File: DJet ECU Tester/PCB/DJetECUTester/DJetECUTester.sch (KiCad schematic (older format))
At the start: 25 parts, among them J1 ISP, J2 ECU, J4 BREAKOUT, J5 12V IN, J6 MPS, U1 ATmega328P, Y1 FA-238 16.0000MB-C3

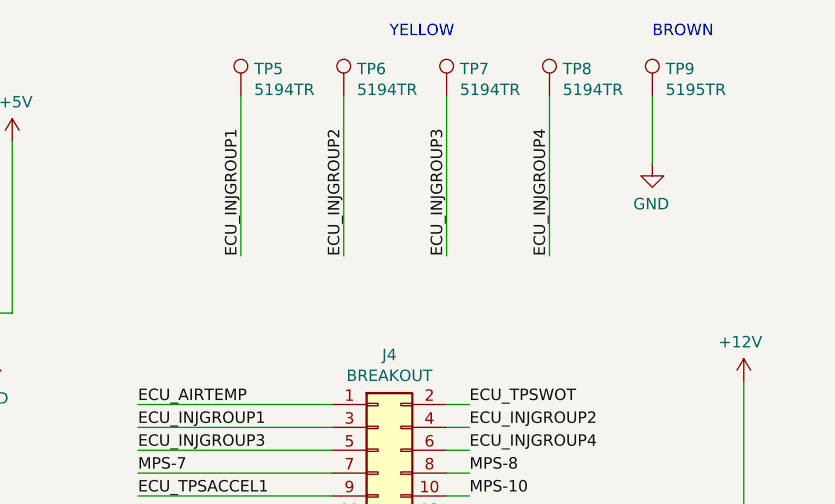
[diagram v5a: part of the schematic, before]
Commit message: Added simulation of injector drivers - only 1-5 group tested.
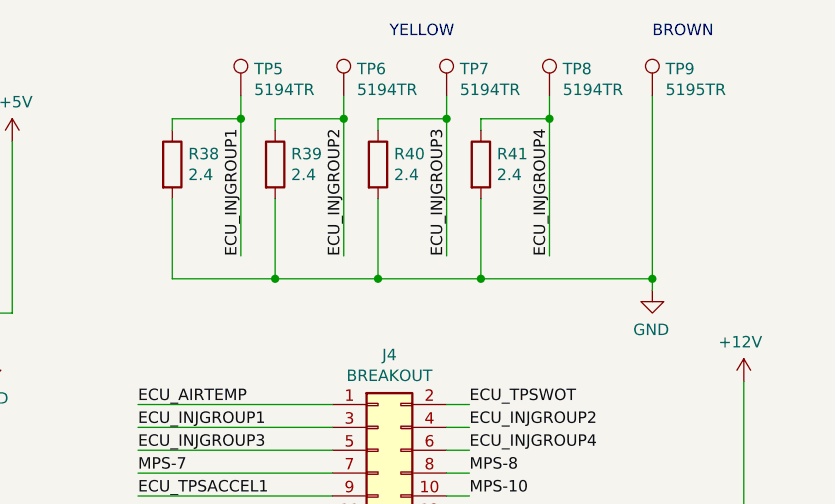
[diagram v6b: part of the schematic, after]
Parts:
- added R38, R39, R40, R41: 2.4, Resistor_SMD:R_0805_2012Metric, symbol Device:R
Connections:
- net ECU_INJGROUP1: now also R38.1
- net ECU_INJGROUP2: now also R39.1
- net ECU_INJGROUP3: now also R40.1
- net ECU_INJGROUP4: now also R41.1
- net GND: now also R38.2, R39.2, R40.2, R41.2
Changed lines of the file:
@@
 L power:GND #PWR053
 U 1 1 60447C04
-P 9650 1200
+P 9650 1750
 AR Path="/60447C04" Ref="#PWR053"  Part="1"
 AR Path="/60479334/60447C04" Ref="#PWR?"  Part="1"
-F 0 "#PWR053" H 9650 950 50  0001 C CNN
-F 1 "GND" H 9655 1027 50  0000 C CNN
-F 2 "" H 9650 1200 50  0001 C CNN
-F 3 "" H 9650 1200 50  0001 C CNN
-	1    9650 1200
+F 0 "#PWR053" H 9650 1500 50  0001 C CNN
+F 1 "GND" H 9655 1577 50  0000 C CNN
+F 2 "" H 9650 1750 50  0001 C CNN
+F 3 "" H 9650 1750 50  0001 C CNN
+	1    9650 1750
 	-1   0    0    -1
 $EndComp
-Wire Wire Line
-	9650 1200 9650 900
 Text Label 7850 1600 1    50   ~ 0
 ECU_INJGROUP1
@@
 ECU_INJGROUP4
 Wire Wire Line
-	7850 900  7850 1600
+	7850 900  7850 1000
 Wire Wire Line
-	8300 900  8300 1600
+	8300 900  8300 1000
 Wire Wire Line
-	8750 900  8750 1600
+	8750 900  8750 1000
 Wire Wire Line
-	9200 900  9200 1600
+	9200 900  9200 1000
 $Sheet
 S 1500 3850 900  300
@@
 Text Notes 8500 650  0    50   ~ 0
 YELLOW
+$Comp
+L Device:R R38
+U 1 1 604C75AB
+P 7550 1200
+F 0 "R38" H 7620 1246 50  0000 L CNN
+F 1 "2.4" H 7620 1155 50  0000 L CNN
+F 2 "Resistor_SMD:R_0805_2012Metric" V 7480 1200 50  0001 C CNN
+F 3 "~" H 7550 1200 50  0001 C CNN
+	1    7550 1200
+	1    0    0    -1
+$EndComp
+Wire Wire Line
+	7850 1000 7550 1000
+Wire Wire Line
+	7550 1000 7550 1050
+Connection ~ 7850 1000
+Wire Wire Line
+	7850 1000 7850 1600
+$Comp
+L Device:R R39
+U 1 1 604D383D
+P 8000 1200
+F 0 "R39" H 8070 1246 50  0000 L CNN
+F 1 "2.4" H 8070 1155 50  0000 L CNN
+F 2 "Resistor_SMD:R_0805_2012Metric" V 7930 1200 50  0001 C CNN
+F 3 "~" H 8000 1200 50  0001 C CNN
+	1    8000 1200
+	1    0    0    -1
+$EndComp
+$Comp
+L Device:R R40
+U 1 1 604D3B92
+P 8450 1200
+F 0 "R40" H 8520 1246 50  0000 L CNN
+F 1 "2.4" H 8520 1155 50  0000 L CNN
+F 2 "Resistor_SMD:R_0805_2012Metric" V 8380 1200 50  0001 C CNN
+F 3 "~" H 8450 1200 50  0001 C CNN
+	1    8450 1200
+	1    0    0    -1
+$EndComp
+$Comp
+L Device:R R41
+U 1 1 604D3F29
+P 8900 1200
+F 0 "R41" H 8970 1246 50  0000 L CNN
+F 1 "2.4" H 8970 1155 50  0000 L CNN
+F 2 "Resistor_SMD:R_0805_2012Metric" V 8830 1200 50  0001 C CNN
+F 3 "~" H 8900 1200 50  0001 C CNN
+	1    8900 1200
+	1    0    0    -1
+$EndComp
+Wire Wire Line
+	8300 1000 8000 1000
+Wire Wire Line
+	8000 1000 8000 1050
+Connection ~ 8300 1000
+Wire Wire Line
+	8300 1000 8300 1600
+Wire Wire Line
+	8750 1000 8450 1000
+Wire Wire Line
+	8450 1000 8450 1050
+Connection ~ 8750 1000
+Wire Wire Line
+	8750 1000 8750 1600
+Wire Wire Line
+	9200 1000 8900 1000
+Wire Wire Line
+	8900 1000 8900 1050
+Connection ~ 9200 1000
+Wire Wire Line
+	9200 1000 9200 1600
+Wire Wire Line
+	9650 900  9650 1700
+Wire Wire Line
+	9650 1700 8900 1700
+Wire Wire Line
+	7550 1700 7550 1350
+Connection ~ 9650 1700
+Wire Wire Line
+	9650 1700 9650 1750
+Wire Wire Line
+	8000 1350 8000 1700
+Connection ~ 8000 1700
+Wire Wire Line
+	8000 1700 7550 1700
+Wire Wire Line
+	8450 1350 8450 1700
+Connection ~ 8450 1700
+Wire Wire Line
+	8450 1700 8000 1700
+Wire Wire Line
+	8900 1350 8900 1700
+Connection ~ 8900 1700
+Wire Wire Line
+	8900 1700 8450 1700
 $EndSCHEMATC

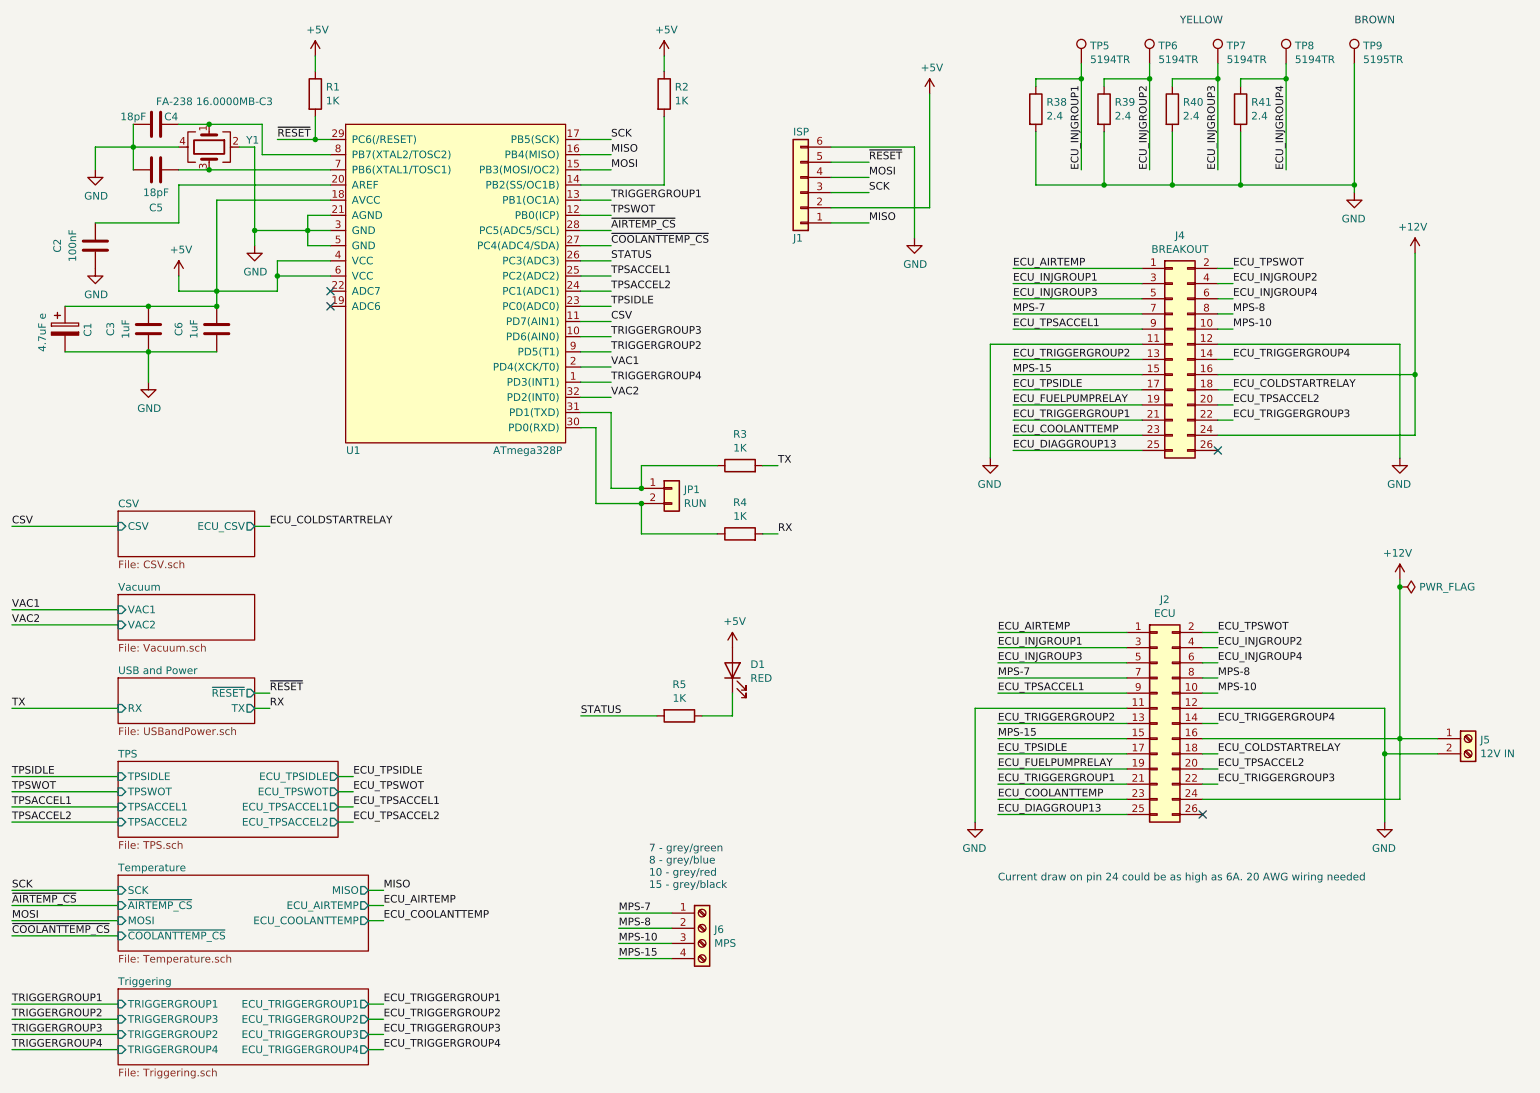
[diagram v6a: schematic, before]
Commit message: Added connector for injector groups.
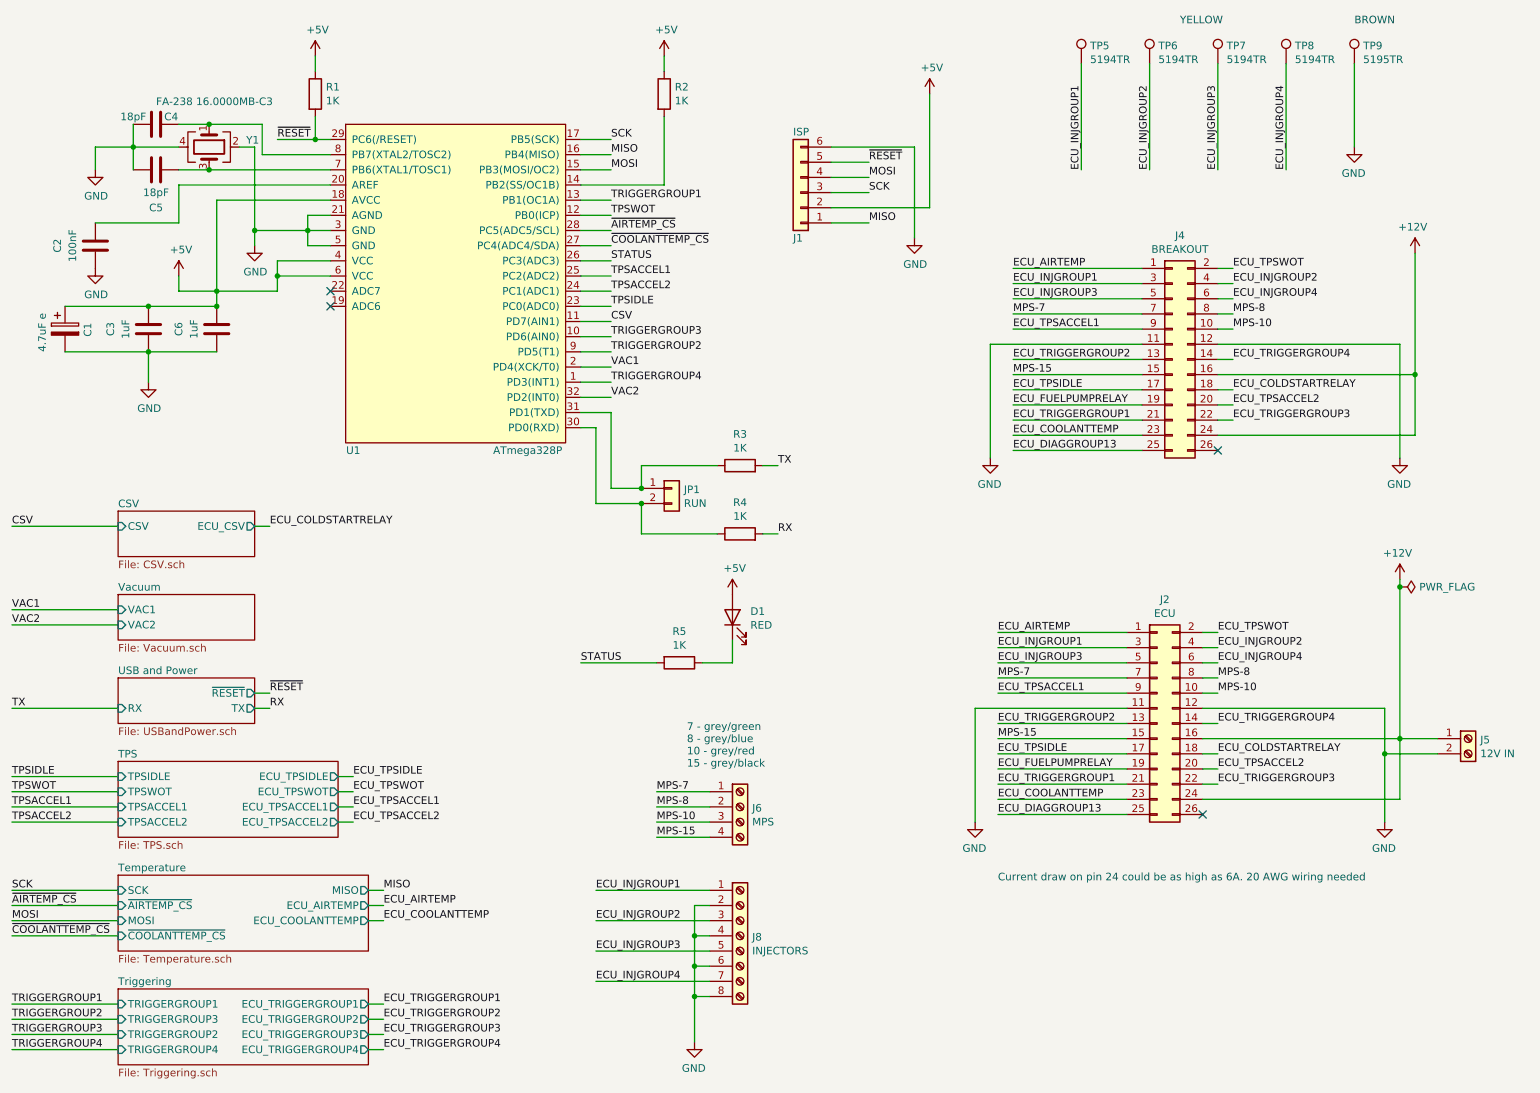
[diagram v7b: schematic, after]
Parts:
- removed R38, R39, R40, R41: 2.4, Resistor_SMD:R_0805_2012Metric, symbol Device:R
- added J8: INJECTORS, TerminalBlock_TE-Connectivity:TerminalBlock_TE_282834-8_1x08_P2.54mm_Horizontal, symbol Connector:Screw_Terminal_01x08
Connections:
- net ECU_INJGROUP1: now also J8.1 (Pin_1)
- net ECU_INJGROUP2: now also J8.3 (Pin_3)
- net ECU_INJGROUP3: now also J8.5 (Pin_5)
- net ECU_INJGROUP4: now also J8.7 (Pin_7)
- net GND: now also J8.2 (Pin_2), J8.4 (Pin_4), J8.6 (Pin_6), J8.8 (Pin_8)
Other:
- moved on the sheet: D1, J6, R5
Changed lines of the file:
@@
 L Device:LED D1
 U 1 1 6003C913
-P 5550 4900
-F 0 "D1" V 5589 4782 50  0000 R CNN
-F 1 "RED" V 5498 4782 50  0000 R CNN
-F 2 "LED_SMD:LED_PLCC-2" H 5550 4900 50  0001 C CNN
-F 3 "~" H 5550 4900 50  0001 C CNN
-	1    5550 4900
+P 5550 4550
+F 0 "D1" V 5589 4432 50  0000 R CNN
+F 1 "RED" V 5498 4432 50  0000 R CNN
+F 2 "LED_SMD:LED_PLCC-2" H 5550 4550 50  0001 C CNN
+F 3 "~" H 5550 4550 50  0001 C CNN
+	1    5550 4550
 	0    -1   -1   0
 $EndComp
@@
 L Device:R R5
 U 1 1 6003D307
-P 5200 5200
-F 0 "R5" V 4993 5200 50  0000 C CNN
-F 1 "1K" V 5084 5200 50  0000 C CNN
-F 2 "Resistor_SMD:R_0805_2012Metric" V 5130 5200 50  0001 C CNN
-F 3 "~" H 5200 5200 50  0001 C CNN
-	1    5200 5200
+P 5200 4850
+F 0 "R5" V 4993 4850 50  0000 C CNN
+F 1 "1K" V 5084 4850 50  0000 C CNN
+F 2 "Resistor_SMD:R_0805_2012Metric" V 5130 4850 50  0001 C CNN
+F 3 "~" H 5200 4850 50  0001 C CNN
+	1    5200 4850
 	0    1    1    0
 $EndComp
@@
 L power:+5V #PWR011
 U 1 1 6003D830
-P 5550 4750
-F 0 "#PWR011" H 5550 4600 50  0001 C CNN
-F 1 "+5V" H 5565 4923 50  0000 C CNN
-F 2 "" H 5550 4750 50  0001 C CNN
-F 3 "" H 5550 4750 50  0001 C CNN
-	1    5550 4750
-	1    0    0    -1
-$EndComp
-Wire Wire Line
-	5550 5050 5550 5200
-Wire Wire Line
-	5550 5200 5350 5200
-Wire Wire Line
-	5050 5200 4550 5200
-Text Label 4550 5200 0    50   ~ 0
+P 5550 4400
+F 0 "#PWR011" H 5550 4250 50  0001 C CNN
+F 1 "+5V" H 5565 4573 50  0000 C CNN
+F 2 "" H 5550 4400 50  0001 C CNN
+F 3 "" H 5550 4400 50  0001 C CNN
+	1    5550 4400
+	1    0    0    -1
+$EndComp
+Wire Wire Line
+	5550 4700 5550 4850
+Wire Wire Line
+	5550 4850 5350 4850
+Wire Wire Line
+	5050 4850 4550 4850
+Text Label 4550 4850 0    50   ~ 0
 STATUS
 $Sheet
@@
 L Connector:Screw_Terminal_01x04 J6
 U 1 1 6044C452
-P 5350 6600
-F 0 "J6" H 5430 6592 50  0000 L CNN
-F 1 "MPS" H 5430 6501 50  0000 L CNN
-F 2 "TerminalBlock_TE-Connectivity:TerminalBlock_TE_282834-4_1x04_P2.54mm_Horizontal" H 5350 6600 50  0001 C CNN
-F 3 "~" H 5350 6600 50  0001 C CNN
-F 4 "282834-4" H 5350 6600 50  0001 C CNN "manf#"
-	1    5350 6600
+P 5600 5800
+F 0 "J6" H 5680 5792 50  0000 L CNN
+F 1 "MPS" H 5680 5701 50  0000 L CNN
+F 2 "TerminalBlock_TE-Connectivity:TerminalBlock_TE_282834-4_1x04_P2.54mm_Horizontal" H 5600 5800 50  0001 C CNN
+F 3 "~" H 5600 5800 50  0001 C CNN
+F 4 "282834-4" H 5600 5800 50  0001 C CNN "manf#"
+	1    5600 5800
 	1    0    0    -1
 $EndComp
@@
 Wire Wire Line
 	7300 5350 8150 5350
-Text Label 4800 6500 0    50   ~ 0
+Text Label 5050 5700 0    50   ~ 0
 MPS-7
-Text Label 4800 6800 0    50   ~ 0
+Text Label 5050 6000 0    50   ~ 0
 MPS-15
-Text Label 4800 6700 0    50   ~ 0
+Text Label 5050 5900 0    50   ~ 0
 MPS-10
-Text Label 4800 6600 0    50   ~ 0
+Text Label 5050 5800 0    50   ~ 0
 MPS-8
 Wire Wire Line
-	4800 6800 5150 6800
-Wire Wire Line
-	5150 6700 4800 6700
-Wire Wire Line
-	4800 6600 5150 6600
-Wire Wire Line
-	5150 6500 4800 6500
-Text Notes 5000 6350 0    50   ~ 0
+	5050 6000 5400 6000
+Wire Wire Line
+	5400 5900 5050 5900
+Wire Wire Line
+	5050 5800 5400 5800
+Wire Wire Line
+	5400 5700 5050 5700
+Text Notes 5250 5550 0    50   ~ 0
 7 - grey/green\n8 - grey/blue\n10 - grey/red\n15 - grey/black
 Wire Wire Line
@@
 L power:GND #PWR053
 U 1 1 60447C04
-P 9650 1750
+P 9650 1450
 AR Path="/60447C04" Ref="#PWR053"  Part="1"
 AR Path="/60479334/60447C04" Ref="#PWR?"  Part="1"
-F 0 "#PWR053" H 9650 1500 50  0001 C CNN
-F 1 "GND" H 9655 1577 50  0000 C CNN
-F 2 "" H 9650 1750 50  0001 C CNN
-F 3 "" H 9650 1750 50  0001 C CNN
-	1    9650 1750
+F 0 "#PWR053" H 9650 1200 50  0001 C CNN
+F 1 "GND" H 9655 1277 50  0000 C CNN
+F 2 "" H 9650 1450 50  0001 C CNN
+F 3 "" H 9650 1450 50  0001 C CNN
+	1    9650 1450
 	-1   0    0    -1
 $EndComp
@@
 Text Label 9200 1600 1    50   ~ 0
 ECU_INJGROUP4
-Wire Wire Line
-	7850 900  7850 1000
-Wire Wire Line
-	8300 900  8300 1000
-Wire Wire Line
-	8750 900  8750 1000
-Wire Wire Line
-	9200 900  9200 1000
 $Sheet
 S 1500 3850 900  300
@@
 Text Notes 8500 650  0    50   ~ 0
 YELLOW
-$Comp
-L Device:R R38
-U 1 1 604C75AB
-P 7550 1200
-F 0 "R38" H 7620 1246 50  0000 L CNN
-F 1 "2.4" H 7620 1155 50  0000 L CNN
-F 2 "Resistor_SMD:R_0805_2012Metric" V 7480 1200 50  0001 C CNN
-F 3 "~" H 7550 1200 50  0001 C CNN
-	1    7550 1200
-	1    0    0    -1
-$EndComp
-Wire Wire Line
-	7850 1000 7550 1000
-Wire Wire Line
-	7550 1000 7550 1050
-Connection ~ 7850 1000
-Wire Wire Line
-	7850 1000 7850 1600
-$Comp
-L Device:R R39
-U 1 1 604D383D
-P 8000 1200
-F 0 "R39" H 8070 1246 50  0000 L CNN
-F 1 "2.4" H 8070 1155 50  0000 L CNN
-F 2 "Resistor_SMD:R_0805_2012Metric" V 7930 1200 50  0001 C CNN
-F 3 "~" H 8000 1200 50  0001 C CNN
-	1    8000 1200
-	1    0    0    -1
-$EndComp
-$Comp
-L Device:R R40
-U 1 1 604D3B92
-P 8450 1200
-F 0 "R40" H 8520 1246 50  0000 L CNN
-F 1 "2.4" H 8520 1155 50  0000 L CNN
-F 2 "Resistor_SMD:R_0805_2012Metric" V 8380 1200 50  0001 C CNN
-F 3 "~" H 8450 1200 50  0001 C CNN
-	1    8450 1200
-	1    0    0    -1
-$EndComp
-$Comp
-L Device:R R41
-U 1 1 604D3F29
-P 8900 1200
-F 0 "R41" H 8970 1246 50  0000 L CNN
-F 1 "2.4" H 8970 1155 50  0000 L CNN
-F 2 "Resistor_SMD:R_0805_2012Metric" V 8830 1200 50  0001 C CNN
-F 3 "~" H 8900 1200 50  0001 C CNN
-	1    8900 1200
-	1    0    0    -1
-$EndComp
-Wire Wire Line
-	8300 1000 8000 1000
-Wire Wire Line
-	8000 1000 8000 1050
-Connection ~ 8300 1000
-Wire Wire Line
-	8300 1000 8300 1600
-Wire Wire Line
-	8750 1000 8450 1000
-Wire Wire Line
-	8450 1000 8450 1050
-Connection ~ 8750 1000
-Wire Wire Line
-	8750 1000 8750 1600
-Wire Wire Line
-	9200 1000 8900 1000
-Wire Wire Line
-	8900 1000 8900 1050
-Connection ~ 9200 1000
-Wire Wire Line
-	9200 1000 9200 1600
-Wire Wire Line
-	9650 900  9650 1700
-Wire Wire Line
-	9650 1700 8900 1700
-Wire Wire Line
-	7550 1700 7550 1350
-Connection ~ 9650 1700
-Wire Wire Line
-	9650 1700 9650 1750
-Wire Wire Line
-	8000 1350 8000 1700
-Connection ~ 8000 1700
-Wire Wire Line
-	8000 1700 7550 1700
-Wire Wire Line
-	8450 1350 8450 1700
-Connection ~ 8450 1700
-Wire Wire Line
-	8450 1700 8000 1700
-Wire Wire Line
-	8900 1350 8900 1700
-Connection ~ 8900 1700
-Wire Wire Line
-	8900 1700 8450 1700
+Wire Wire Line
+	7850 900  7850 1600
+Wire Wire Line
+	8300 900  8300 1600
+Wire Wire Line
+	8750 900  8750 1600
+Wire Wire Line
+	9200 900  9200 1600
+Wire Wire Line
+	9650 900  9650 1450
+$Comp
+L Connector:Screw_Terminal_01x08 J8
+U 1 1 60530292
+P 5600 6650
+F 0 "J8" H 5680 6642 50  0000 L CNN
+F 1 "INJECTORS" H 5680 6551 50  0000 L CNN
+F 2 "TerminalBlock_TE-Connectivity:TerminalBlock_TE_282834-8_1x08_P2.54mm_Horizontal" H 5600 6650 50  0001 C CNN
+F 3 "~" H 5600 6650 50  0001 C CNN
+	1    5600 6650
+	1    0    0    -1
+$EndComp
+Text Label 4650 6350 0    50   ~ 0
+ECU_INJGROUP1
+Text Label 4650 6550 0    50   ~ 0
+ECU_INJGROUP2
+Text Label 4650 6750 0    50   ~ 0
+ECU_INJGROUP3
+Text Label 4650 6950 0    50   ~ 0
+ECU_INJGROUP4
+Wire Wire Line
+	4650 6950 5400 6950
+Wire Wire Line
+	5400 6750 4650 6750
+Wire Wire Line
+	4650 6550 5400 6550
+Wire Wire Line
+	5400 6350 4650 6350
+$Comp
+L power:GND #PWR044
+U 1 1 60560B4D
+P 5300 7350
+AR Path="/60560B4D" Ref="#PWR044"  Part="1"
+AR Path="/60479334/60560B4D" Ref="#PWR?"  Part="1"
+F 0 "#PWR044" H 5300 7100 50  0001 C CNN
+F 1 "GND" H 5305 7177 50  0000 C CNN
+F 2 "" H 5300 7350 50  0001 C CNN
+F 3 "" H 5300 7350 50  0001 C CNN
+	1    5300 7350
+	-1   0    0    -1
+$EndComp
+Wire Wire Line
+	5300 7350 5300 7050
+Wire Wire Line
+	5300 6450 5400 6450
+Wire Wire Line
+	5400 6650 5300 6650
+Connection ~ 5300 6650
+Wire Wire Line
+	5300 6650 5300 6450
+Wire Wire Line
+	5300 6850 5400 6850
+Connection ~ 5300 6850
+Wire Wire Line
+	5300 6850 5300 6650
+Wire Wire Line
+	5400 7050 5300 7050
+Connection ~ 5300 7050
+Wire Wire Line
+	5300 7050 5300 6850
 $EndSCHEMATC

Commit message: Updated manufacturer part numbers. Working on ECU outputs tester board.
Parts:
- J2: manf# (none) -> BC-32677
- J8: manf# (none) -> 282834-8
- U1: manf# (none) -> ATMEGA328P-AUR
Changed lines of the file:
@@
 F 2 "Package_QFP:LQFP-32_7x7mm_P0.8mm" H 1750 2700 50  0001 C CNN
 F 3 "" H 1750 2700 50  0001 C CNN
+F 4 "ATMEGA328P-AUR" H 3000 3400 50  0001 C CNN "manf#"
 	1    3000 3400
 	1    0    0    -1
@@
 F 2 "Connector_IDC:IDC-Header_2x13_P2.54mm_Vertical" H 8350 5250 50  0001 C CNN
 F 3 "~" H 8350 5250 50  0001 C CNN
+F 4 "BC-32677" H 8350 5250 50  0001 C CNN "manf#"
 	1    8350 5250
 	1    0    0    -1
@@
 F 2 "TerminalBlock_TE-Connectivity:TerminalBlock_TE_282834-8_1x08_P2.54mm_Horizontal" H 5600 6650 50  0001 C CNN
 F 3 "~" H 5600 6650 50  0001 C CNN
+F 4 "282834-8" H 5600 6650 50  0001 C CNN "manf#"
 	1    5600 6650
 	1    0    0    -1
